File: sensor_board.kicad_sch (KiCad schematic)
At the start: 42 parts, among them J5 TagConnect_TC2030_SWD, U1 AMS1117-3.3, U16 7408, U2 STM32H753IITx

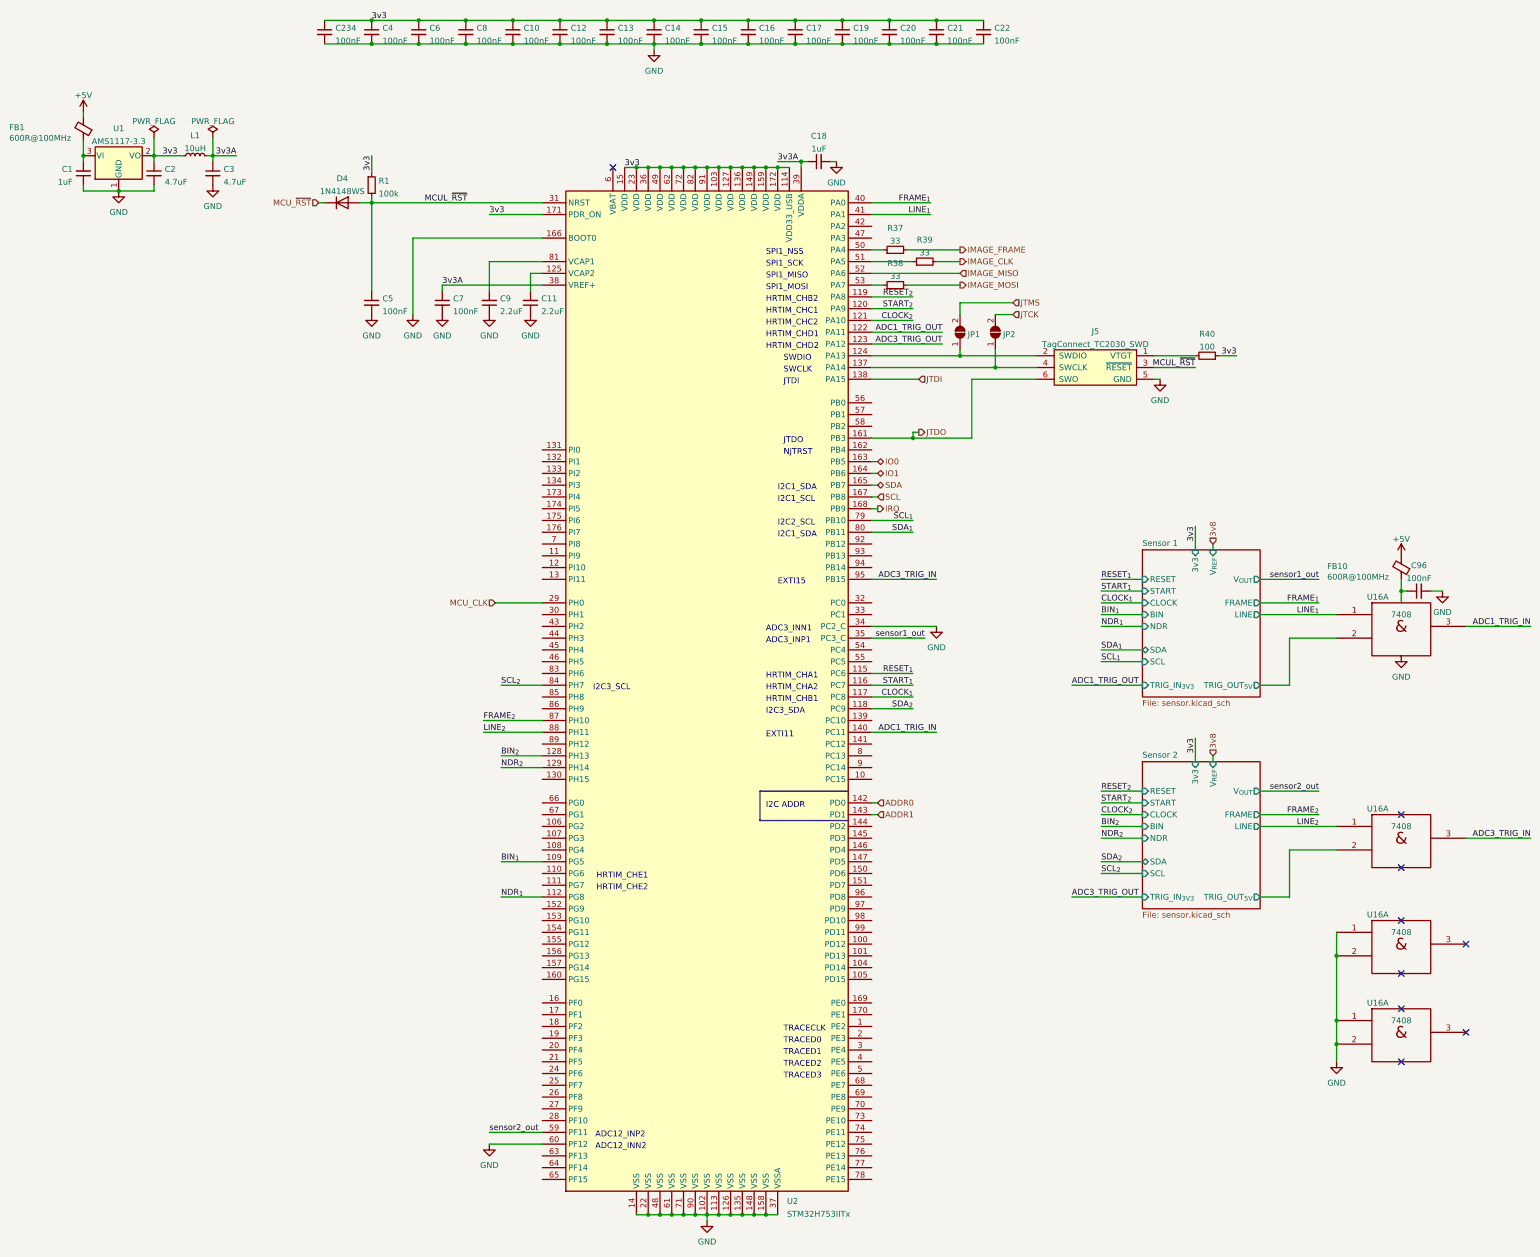
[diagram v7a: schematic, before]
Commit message: Add sensor board power planes
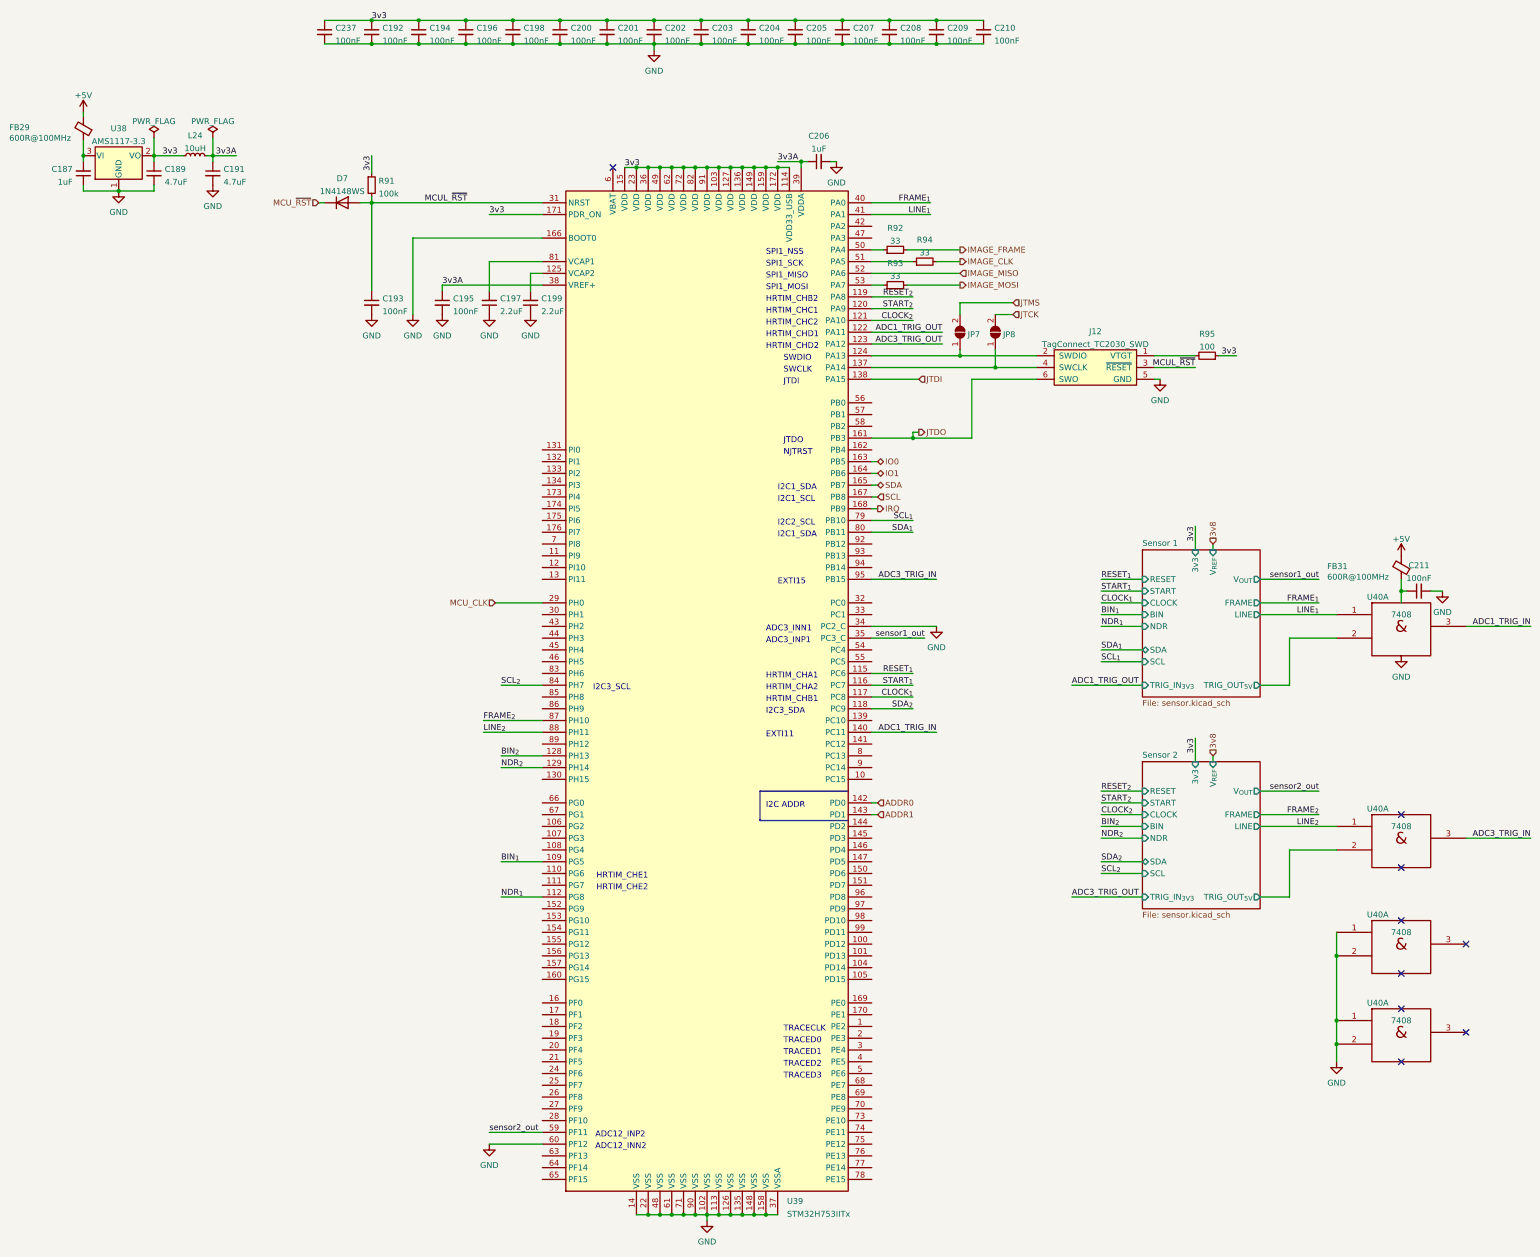
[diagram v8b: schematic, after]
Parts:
- renumbered C1 to C187, C2 to C189, C3 to C191, C4 to C192, C5 to C193, C6 to C194, C7 to C195, C8 to C196, C9 to C197, C10 to C198, C11 to C199, C12 to C200, C13 to C201, C14 to C202, C15 to C203, C16 to C204, C17 to C205, C18 to C206, C19 to C207, C20 to C208, C21 to C209, C22 to C210, C96 to C211, C234 to C237, D4 to D7, FB1 to FB29, FB10 to FB31, J5 to J12, JP1 to JP7, JP2 to JP8, L1 to L24, R1 to R91, R37 to R92, R38 to R93, R39 to R94, R40 to R95, U1 to U38, U2 to U39, U16 to U40
